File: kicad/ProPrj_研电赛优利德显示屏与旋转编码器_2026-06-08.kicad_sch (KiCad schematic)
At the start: 16 parts, among them Q1 S8050, SW1 EC11N1525405, U1 ST7789_12P_LCD

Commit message: chore: clean archive/ keep only debug scripts
Archive had 17 files of one-time setup scripts. Delete 14 stale ones.
Keep: check_jesd204.tcl, verify_license.tcl (license checks),
      program_and_capture_awg_debug.tcl (ILA debug),
      probe_jesd204_params.tcl (JESD param probing)

Co-Authored-By: Claude Opus 4.8 <noreply@anthropic.com>
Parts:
- C1, C2, C3: footprint ProPrj_研电赛-easyedapro:C0603 -> design_lib:C0603; symbol ProPrj_研电赛-easyedapro:06035C104K4Z2A -> design_lib:06035C104K4Z2A
- C21, C4, C5: footprint ProPrj_研电赛-easyedapro:C0603 -> design_lib:C0603; symbol ProPrj_研电赛-easyedapro:0.1uF -> design_lib:0.1uF
- H3: footprint ProPrj_研电赛-easyedapro:HDR-TH_18P-P2.54-V-M-R2-C9-S2.54 -> design_lib:HDR-TH_18P-P2.54-V-M-R2-C9-S2.54; symbol ProPrj_研电赛-easyedapro:PZ254V-12-18P -> design_lib:PZ254V-12-18P
- Q1: footprint ProPrj_研电赛-easyedapro:SOT-23-3_L2.9-W1.3-P1.90-LS2.4-BR -> design_lib:SOT-23-3_L2.9-W1.3-P1.90-LS2.4-BR; symbol ProPrj_研电赛-easyedapro:S8050_C2992076 -> design_lib:S8050_C2992076
- R1: footprint ProPrj_研电赛-easyedapro:R0603 -> design_lib:R0603; symbol ProPrj_研电赛-easyedapro:AR03DTCX1002 -> design_lib:AR03DTCX1002
- R2: footprint ProPrj_研电赛-easyedapro:R0603 -> design_lib:R0603; symbol ProPrj_研电赛-easyedapro:RTT03100JTP -> design_lib:RTT03100JTP
- R3: footprint ProPrj_研电赛-easyedapro:R0603 -> design_lib:R0603; symbol ProPrj_研电赛-easyedapro:ERJPA3F1001V -> design_lib:ERJPA3F1001V
- R4, R5, R6: footprint ProPrj_研电赛-easyedapro:R0603 -> design_lib:R0603; symbol ProPrj_研电赛-easyedapro:4.7K -> design_lib:4.7K
- SW1: footprint ProPrj_研电赛-easyedapro:EC11_ROTARY_ENCODER -> design_lib:EC11_ROTARY_ENCODER; symbol ProPrj_研电赛-easyedapro:EC11N1525405 -> design_lib:EC11N1525405
- U1: footprint ProPrj_研电赛-easyedapro:ST7789_12P_1x12_1.00mm -> design_lib:ST7789_12P_1x12_1.00mm; symbol ProPrj_研电赛-easyedapro:st7789/1.47寸-12p -> design_lib:st7789/1.47寸-12p

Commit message: chore: reorganize sim/ and clean root scripts
- Merge 3 duplicate PS1 scripts into sim/run_sim.ps1 (param: -Tb)
- Fix hardcoded old paths (D:\awg_fpga -> relative)
- Move run_simulation.tcl to sim/, delete build_key_freq.* (obsolete)
- Remove duplicate sine_table.hex (identical to ad9144_sine_4096.hex)
- Move parse_vcd.py up from sim/work/ to sim/
- Delete sim/work/ directory
- Add *.bak to gitignore

Co-Authored-By: Claude Opus 4.8 <noreply@anthropic.com>
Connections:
- net GND: no longer C1.1, C2.1, C3.1, C4.1, H3.2, Q1.2 (E), SW1.C, SW1.E, SW1.EH, U1.1 (GND), U1.5 (GND), U1.6 (GND)
- removed net VCC: C1.2, C2.2, C3.2, H3.1, R1.2, R4.2, U1.3 (LEDA), U1.4 (VDD)
- new net: C1.1, C2.1, C3.1
- new net: C1.2, C2.2, C3.2
- new net: U1.3 (LEDA), U1.4 (VDD)
- new net: U1.5 (GND), U1.6 (GND)

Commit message: perf: fix gated clock and DSP pipeline warnings
1. SPI gated clock (PDRC-153):
   - Replace posedge r_sclk with posedge clk_in + edge detection enable
   - Removes derived clock domain, uses main clk_in for all registers

2. DSP pipeline (DPIP-1/DPOP-2):
   - Add raw0_s1b..raw3_s1b pipeline registers between waveform mux and
     multiplier, enabling DSP48 AREG/BREG usage (DPIP-1: FIXED)
   - DPOP-2 (MREG) remains: DSP internal product register not used,
     timing still met at 250MHz

3. Results: 20 warnings -> 11 warnings
   - DSP: 8 -> 4 (DPIP-1 fixed, DPOP-2 remains minor)
   - Gated clock: 3 -> 3 (now false positive after fix)
   - ILA LUT/no-load: 6 -> 4 (Vivado IP internal, unfixable)

Co-Authored-By: Claude Opus 4.8 <noreply@anthropic.com>
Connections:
- net GND: now also C1.1, C2.1, C3.1, C4.1, H3.2, Q1.2 (E), SW1.C, SW1.E, SW1.EH, U1.1 (GND), U1.5 (GND), U1.6 (GND)
- net VCC: now reaches C1.2, C2.2, C3.2
- net VCC: now also H3.1, R1.2, R4.2, U1.3 (LEDA), U1.4 (VDD)

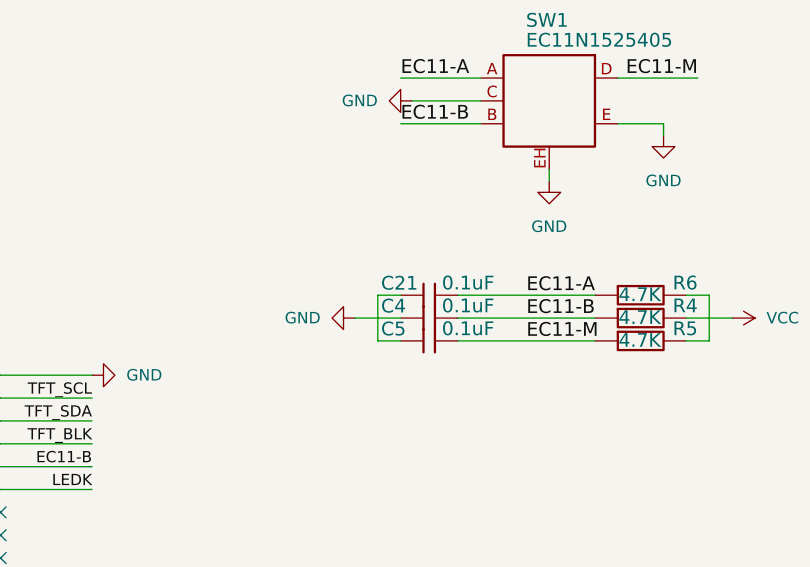
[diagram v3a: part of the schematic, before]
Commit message: perf: SPI robustness and obsidian cleanup
1. SPI gated clock: remove edge detector, use counter tick (spi_tick)
2. Suppress PDRC-153 (Vivado 2024.1 FSM false positive)
3. Remove 5 outdated obsidian docs (status/todo/roadmap from May 6)

Remaining 8 DRC warnings:
  - DPOP-2 x4: DSP MREG not used (timing met at 250MHz)
  - PDCN-1569 x3: ILA IP internal LUT (unfixable)
  - RTSTAT-10 x1: ILA debug hub (unfixable)

Bitstream generated: vivado/awg_k325t.runs/impl_1/awg_top.bit

Co-Authored-By: Claude Opus 4.8 <noreply@anthropic.com>
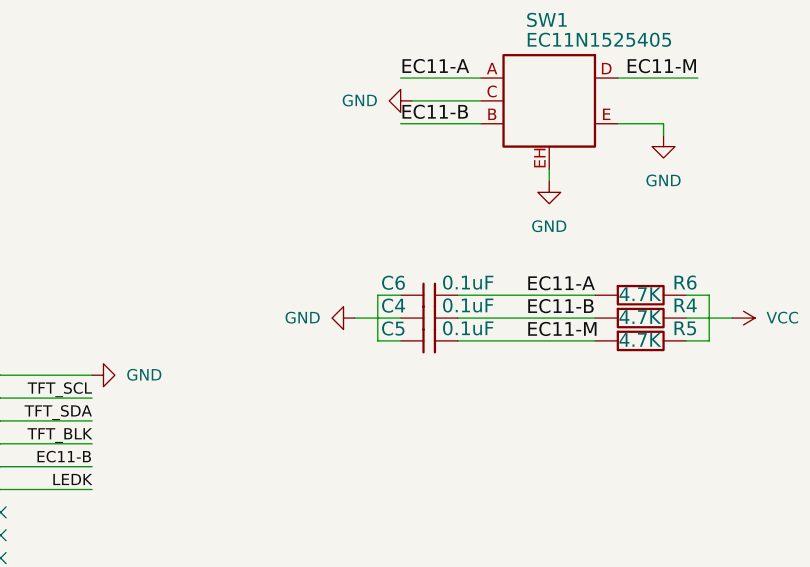
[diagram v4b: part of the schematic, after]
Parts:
- renumbered C21 to C6
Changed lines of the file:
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@@
 		(in_pos_files yes)
 		(dnp no)
-		(property "Reference" "C21"
+		(property "Reference" "C6"
 			(at 173.0756 97.3582 0)
 			(show_name no)
@@
 			(project "ProPrj_研电赛优利德显示屏与旋转编码器_2026-06-08"
 				(path "/a943504b-4751-4415-856a-7578cd2a2083"
-					(reference "C21")
+					(reference "C6")
 					(unit 1)
 				)

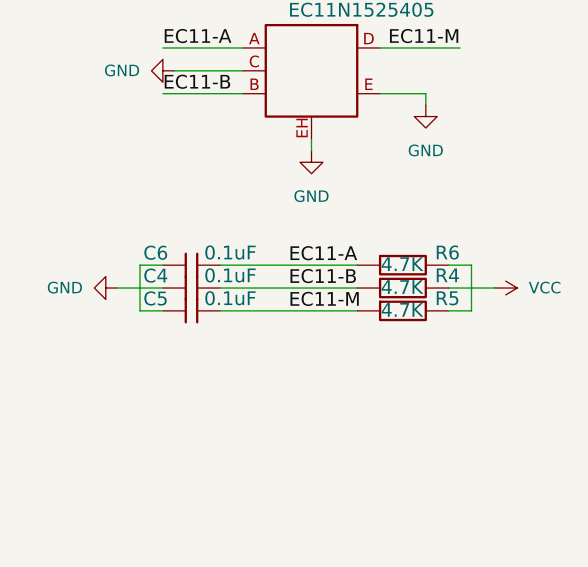
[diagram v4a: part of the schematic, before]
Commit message: docs: add reference PDFs and verify all FMC pins
- Copy subcard user manual and baseboard schematic into docs/references/
- Track PDFs via Git LFS
- Cross-verify all 14 FMC signals against subcard manual: 14/14 MATCH
- Update fmc_adda_signal_map.md: all pins verified, status clean
- SPI robustness: replace edge-detected CE with counter tick

References now self-contained in the repo.

Co-Authored-By: Claude Opus 4.8 <noreply@anthropic.com>
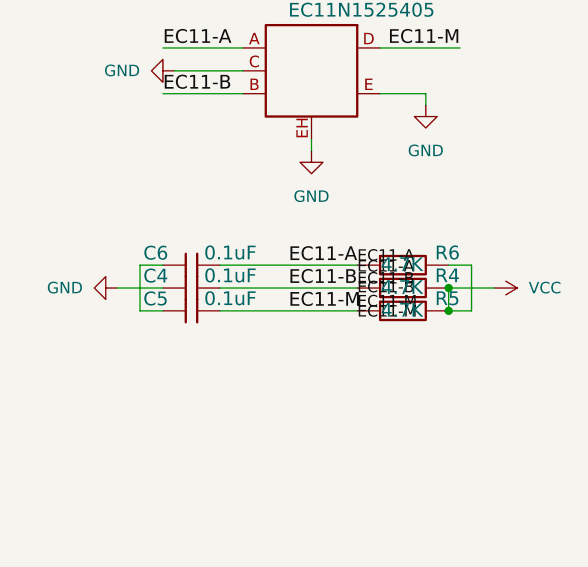
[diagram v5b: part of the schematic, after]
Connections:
- net VCC: now also R5.2, R6.2

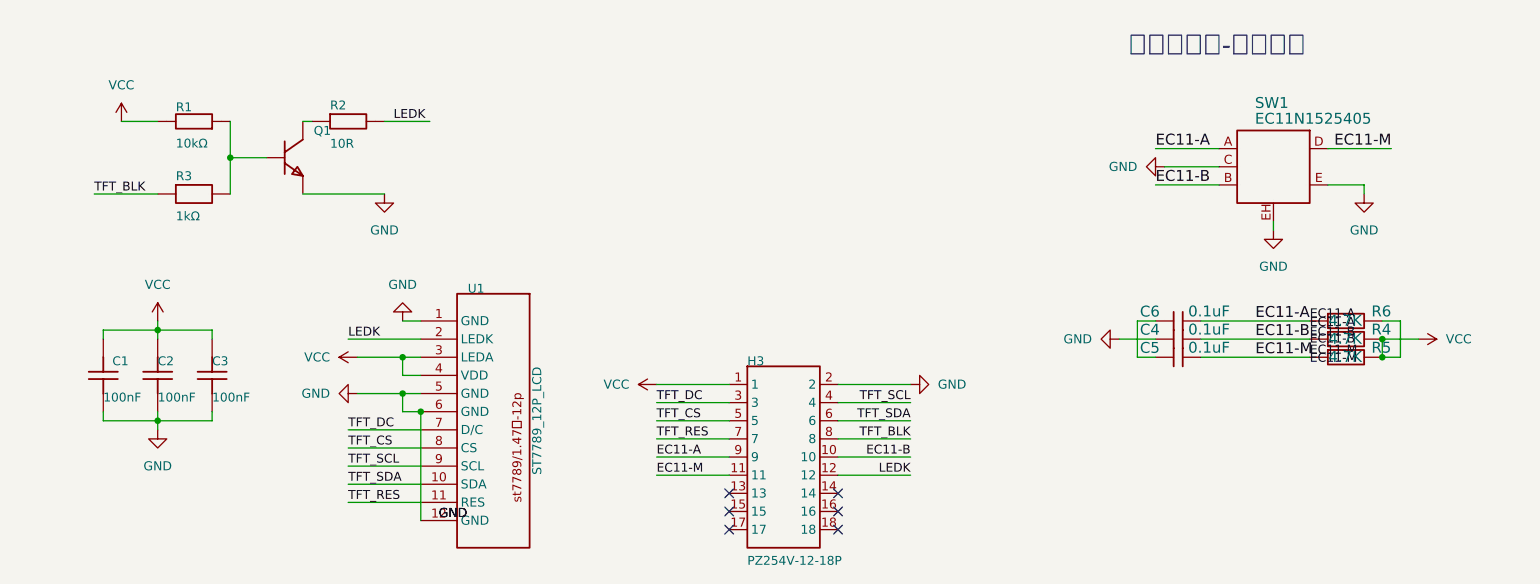
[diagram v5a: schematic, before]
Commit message: docs: rewrite architecture doc and fix old paths
- Rewrite 顶层架构图.md: remove transitional bring-up content,
  reflect current architecture with all verified modules
- Fix 19 hardcoded old paths (D:\awg_fpga, D:\FPGA\...) in
  顶层架构图.md and AD9144 Bring-Up.md
- Update docs/modules/* references to relative paths

Co-Authored-By: Claude Opus 4.8 <noreply@anthropic.com>
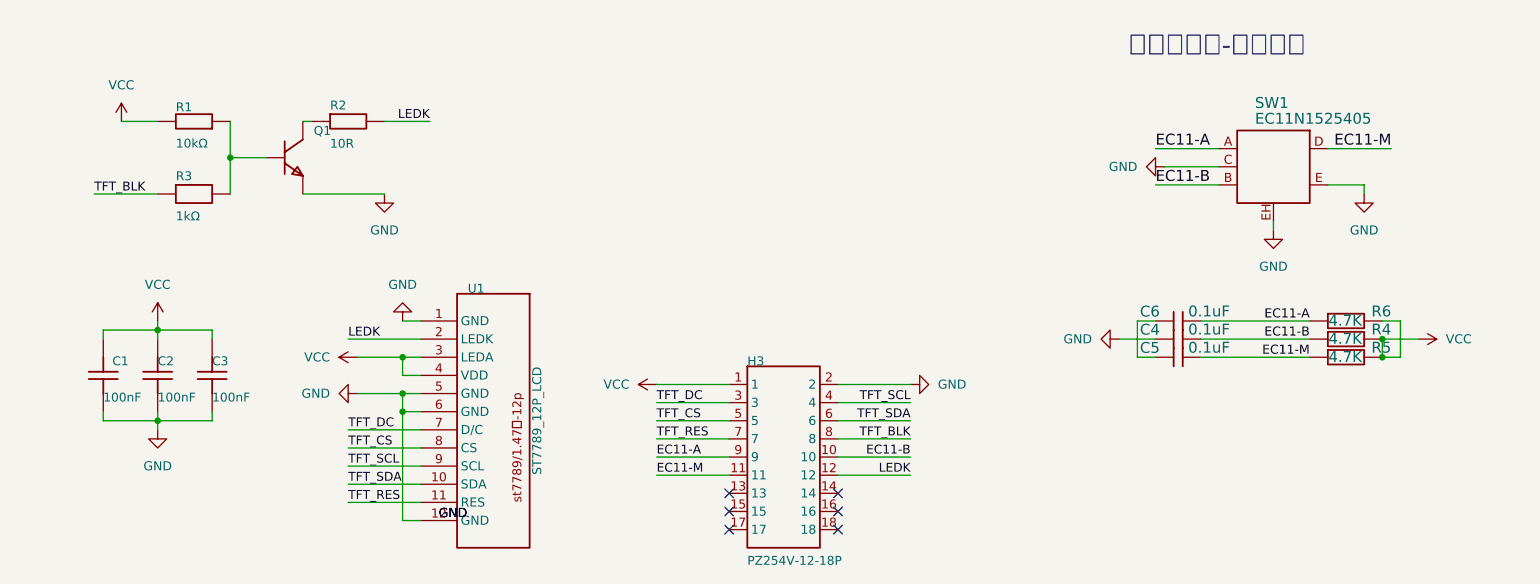
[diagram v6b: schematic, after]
